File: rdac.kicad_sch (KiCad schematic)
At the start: 14 parts

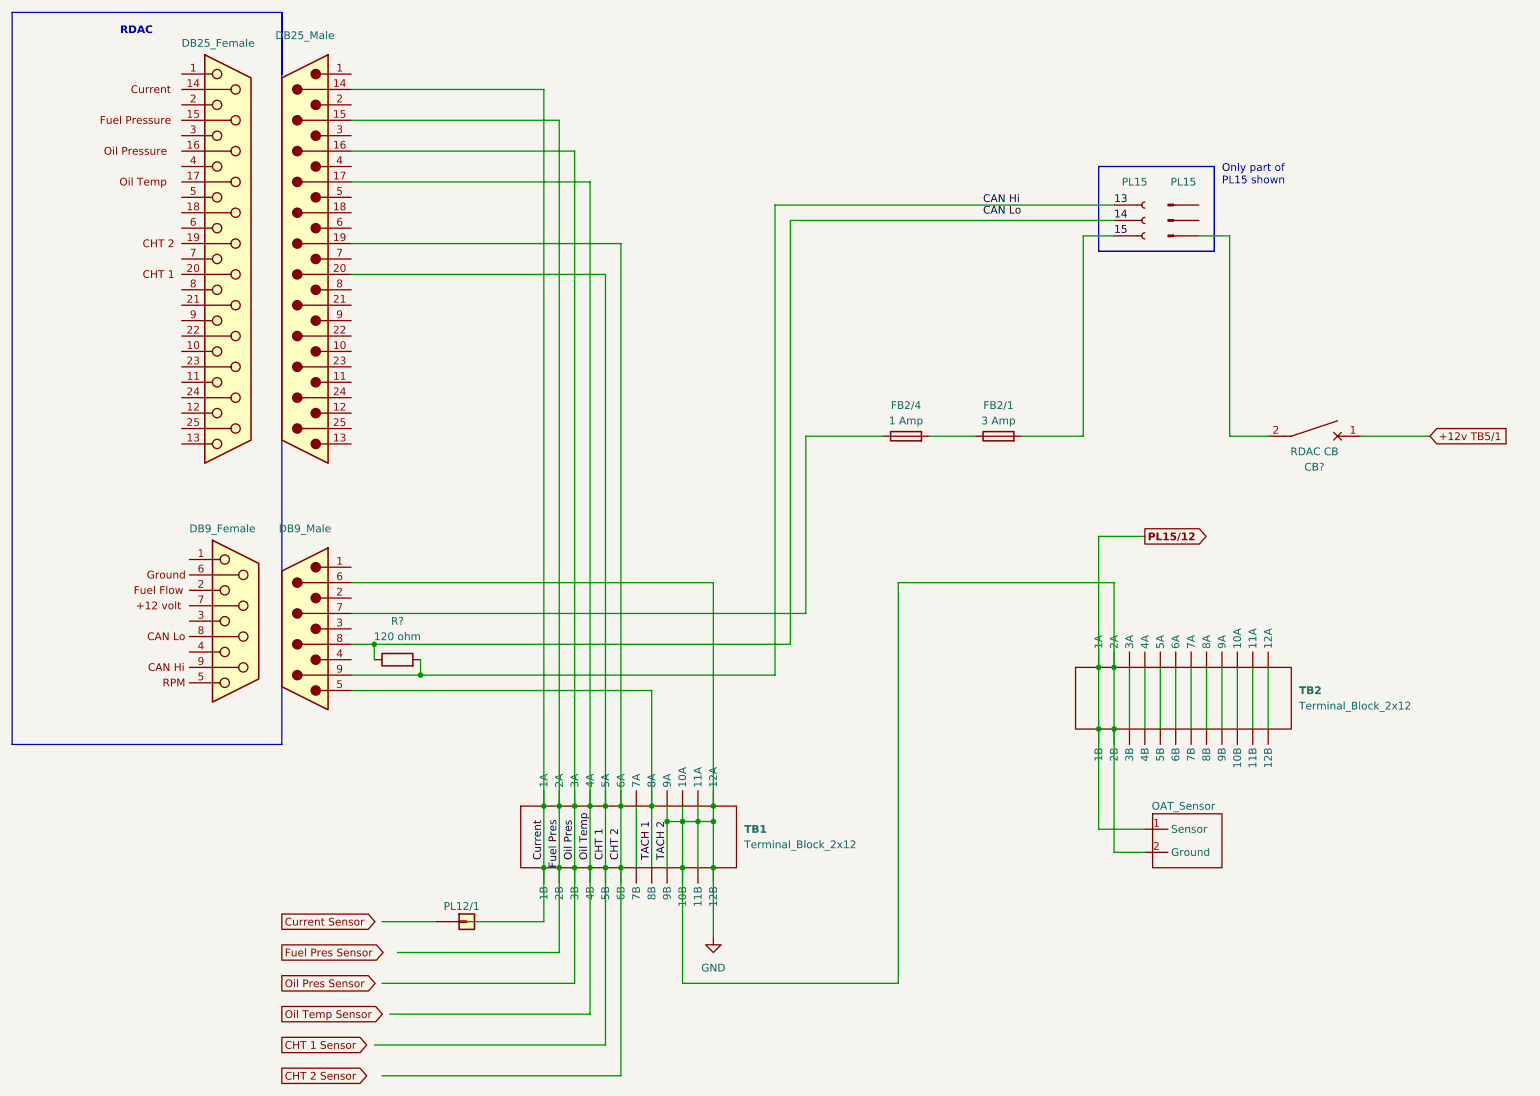
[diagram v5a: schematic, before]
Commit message: Added Fuel Flow Sensor
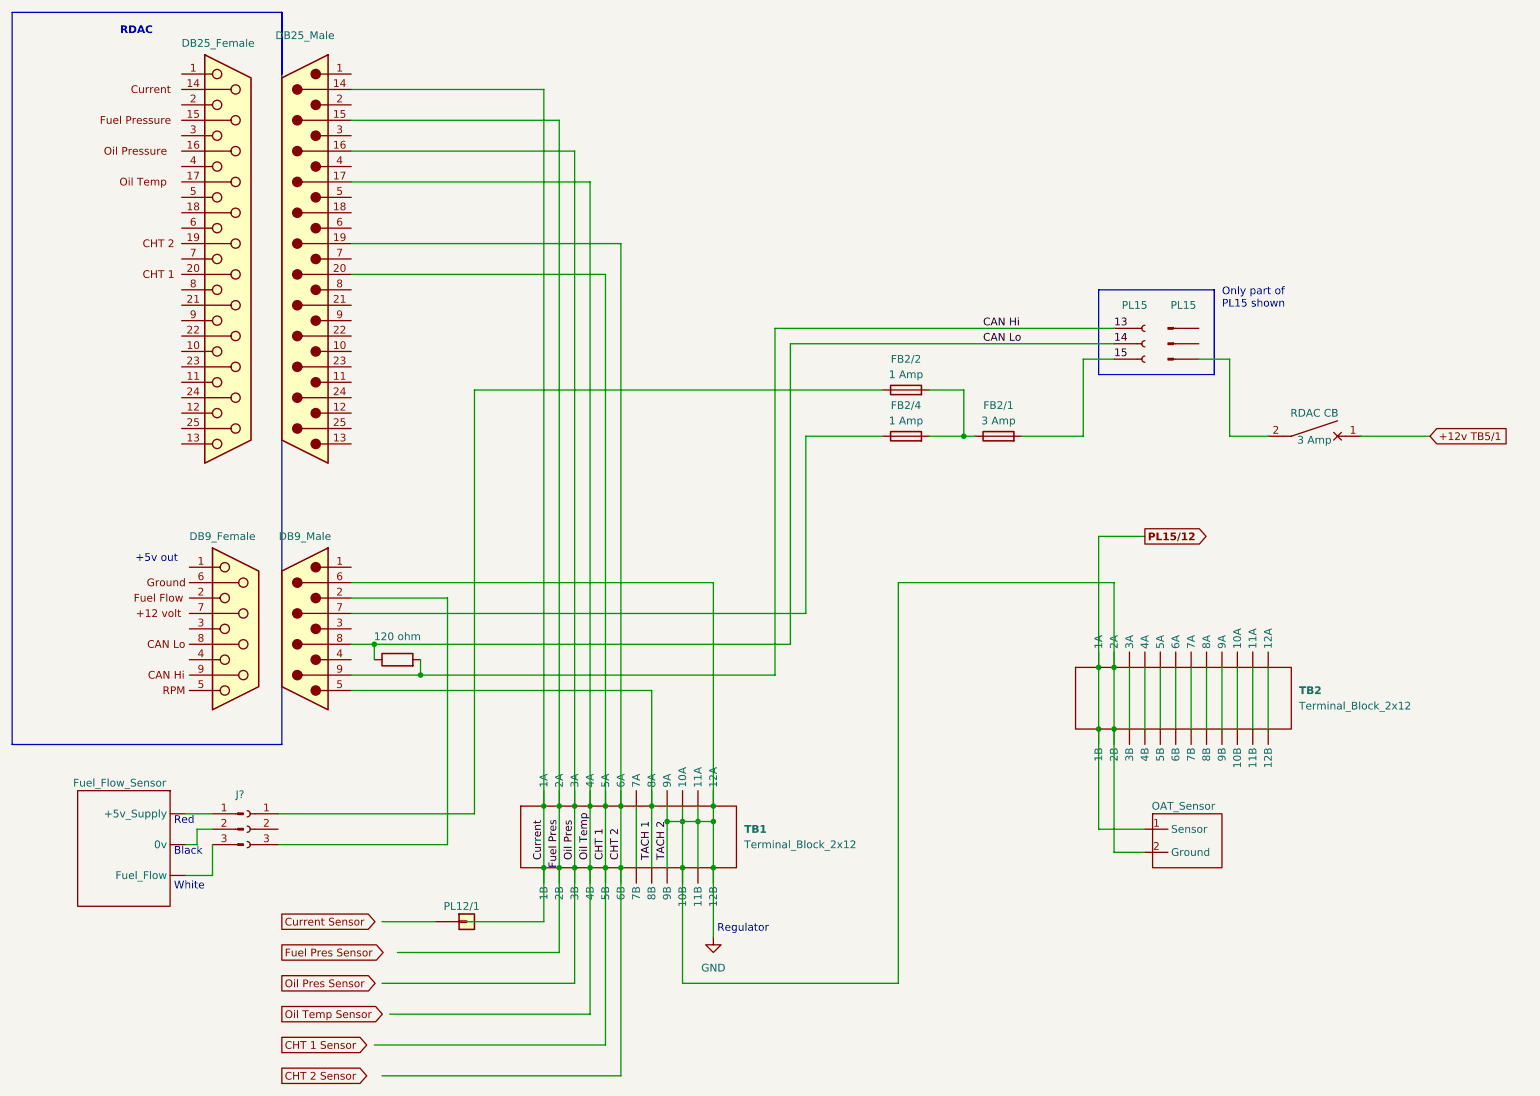
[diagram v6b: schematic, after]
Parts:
- added FB2/2: Fuse, symbol Device:Fuse
- added J?: Conn_01x03_Male, symbol Connector:Conn_01x03_Male
- added J?: Conn_01x03_Female, symbol Connector:Conn_01x03_Female
- added U?: Fuel_Flow_Sensor, symbol gary aircraft symbol library:Fuel_Flow_Sensor
- CB?: Rating (none) -> 3 Amp
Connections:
- net at FB2/1.1, FB2/4.2: now also FB2/2.2
- net at J?.2: now also J?.3 (Pin_3)
- new net: J?.1 (Pin_1), U?. (Fuel_Flow)
- new net: J?.2 (Pin_2), U?. (Fuel_Flow)
- new net: J?.3 (Pin_3), U?. (Fuel_Flow)
- new net: FB2/2.1, J?.1 (Pin_1)
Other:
- note added: "+5v out"
- note added: "Black"
- note added: "Red"
- note added: "Regulator"
- note added: "White"
- moved on the sheet: PL15

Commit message: Added Fuel Flow sensor to RDAC sheet
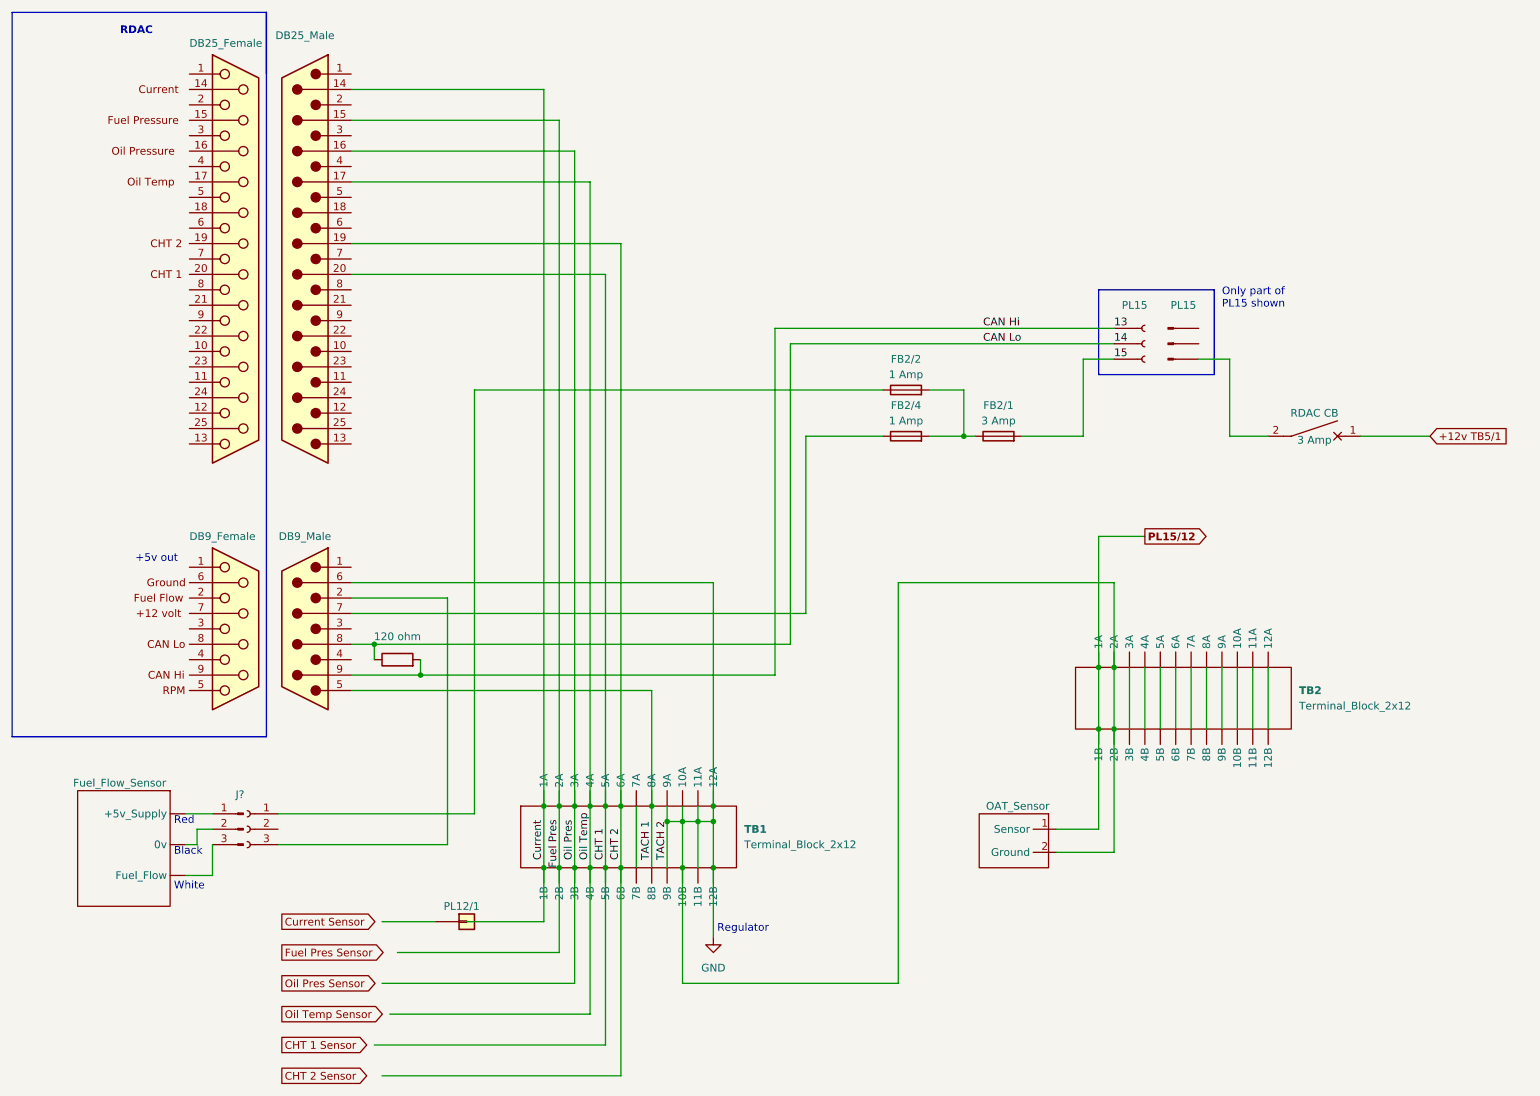
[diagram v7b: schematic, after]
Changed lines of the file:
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@@
     (stroke (width 0) (type dot) (color 0 0 0 0))
-  )
-  (wire (pts (xy 203.2 154.94) (xy 208.28 154.94))
-    (stroke (width 0) (type default) (color 0 0 0 0))
   )
   (wire (pts (xy 81.28 120.65) (xy 149.86 120.65))
@@
     (stroke (width 0) (type default) (color 0 0 0 0))
   )
-  (polyline (pts (xy 66.04 16.51) (xy 66.04 137.16))
+  (polyline (pts (xy 63.5 16.51) (xy 63.5 135.89))
     (stroke (width 0) (type default) (color 0 0 0 0))
   )
@@
     (stroke (width 0) (type default) (color 0 0 0 0))
   )
-  (polyline (pts (xy 21.59 16.51) (xy 21.59 137.16))
+  (polyline (pts (xy 21.59 16.51) (xy 21.59 135.89))
     (stroke (width 0) (type default) (color 0 0 0 0))
   )
@@
     (stroke (width 0) (type dot) (color 0 0 0 0))
   )
-  (polyline (pts (xy 66.04 16.51) (xy 21.59 16.51))
+  (polyline (pts (xy 63.5 16.51) (xy 21.59 16.51))
     (stroke (width 0) (type default) (color 0 0 0 0))
   )
@@
     (stroke (width 0) (type default) (color 0 0 0 0))
   )
-  (polyline (pts (xy 66.04 26.67) (xy 66.04 16.51))
+  (polyline (pts (xy 63.5 26.67) (xy 63.5 16.51))
     (stroke (width 0) (type default) (color 0 0 0 0))
   )
@@
     (stroke (width 0) (type default) (color 0 0 0 0))
   )
+  (wire (pts (xy 193.675 151.13) (xy 200.66 151.13))
+    (stroke (width 0) (type default) (color 0 0 0 0))
+  )
   (wire (pts (xy 97.79 148.59) (xy 97.79 78.74))
     (stroke (width 0) (type default) (color 0 0 0 0))
@@
     (stroke (width 0) (type dot) (color 0 0 0 0))
   )
-  (wire (pts (xy 200.66 151.13) (xy 208.28 151.13))
-    (stroke (width 0) (type default) (color 0 0 0 0))
-  )
   (wire (pts (xy 200.66 124.46) (xy 200.66 102.87))
     (stroke (width 0) (type default) (color 0 0 0 0))
@@
     (stroke (width 0) (type default) (color 0 0 0 0))
   )
-  (polyline (pts (xy 21.59 137.16) (xy 66.04 137.16))
+  (polyline (pts (xy 21.59 135.89) (xy 63.5 135.89))
     (stroke (width 0) (type default) (color 0 0 0 0))
   )
@@
   )
   (wire (pts (xy 77.47 113.03) (xy 93.345 113.03))
+    (stroke (width 0) (type default) (color 0 0 0 0))
+  )
+  (wire (pts (xy 193.675 154.94) (xy 203.2 154.94))
     (stroke (width 0) (type default) (color 0 0 0 0))
   )
@@
     (pin "1")
   )
-  (symbol (lib_id "gary aircraft symbol library:OAT_Sensor") (at 214.63 146.05 0) (unit 1)
+  (symbol (lib_id "gary aircraft symbol library:OAT_Sensor") (at 187.325 146.05 0) (mirror y) (unit 1)
     (in_bom yes) (on_board no)
-    (property "Reference" "U?" (id 0) (at 214.63 144.78 0)
-      (effects (font (size 1.27 1.27)) hide)
-    )
-    (property "Value" "OAT_Sensor" (id 1) (at 214.63 147.32 0))
-    (property "Footprint" "" (id 2) (at 214.63 146.05 0)
-      (effects (font (size 1.27 1.27)) hide)
-    )
-    (property "Datasheet" "" (id 3) (at 214.63 146.05 0)
+    (property "Reference" "U?" (id 0) (at 187.325 144.78 0)
+      (effects (font (size 1.27 1.27)) hide)
+    )
+    (property "Value" "OAT_Sensor" (id 1) (at 187.325 147.32 0))
+    (property "Footprint" "" (id 2) (at 187.325 146.05 0)
+      (effects (font (size 1.27 1.27)) hide)
+    )
+    (property "Datasheet" "" (id 3) (at 187.325 146.05 0)
       (effects (font (size 1.27 1.27)) hide)
     )
@@
     (pin "3")
   )
-  (symbol (lib_id "Connector:DB25_Female") (at 57.15 57.15 0) (unit 1)
-    (in_bom yes) (on_board yes)
-    (property "Reference" "J?" (id 0) (at 54.61 19.05 0)
-      (effects (font (size 1.27 1.27)) (justify left) hide)
-    )
-    (property "Value" "DB25_Female" (id 1) (at 49.53 21.59 0)
+  (symbol (lib_id "Connector:DB25_Female") (at 58.42 57.15 0) (unit 1)
+    (in_bom yes) (on_board yes)
+    (property "Reference" "J?" (id 0) (at 55.88 19.05 0)
+      (effects (font (size 1.27 1.27)) (justify left) hide)
+    )
+    (property "Value" "DB25_Female" (id 1) (at 50.8 21.59 0)
       (effects (font (size 1.27 1.27)) (justify left))
     )
-    (property "Footprint" "" (id 2) (at 57.15 57.15 0)
-      (effects (font (size 1.27 1.27)) hide)
-    )
-    (property "Datasheet" " ~" (id 3) (at 57.15 57.15 0)
-      (effects (font (size 1.27 1.27)) hide)
-    )
+    (property "Footprint" "" (id 2) (at 58.42 57.15 0)
+      (effects (font (size 1.27 1.27)) hide)
+    )
+    (property "Datasheet" " ~" (id 3) (at 58.42 57.15 0)
+      (effects (font (size 1.27 1.27)) hide)
+    )
